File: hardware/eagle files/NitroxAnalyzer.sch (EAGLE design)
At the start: 16 parts

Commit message: Updated a bit the buttons hardware board to better match the 3d box
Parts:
- removed JP1: (no value), pinhead:PINHD-1X4
- removed JP11: (no value), pinhead:PINHD-1X3
- removed JP3, JP4: (no value), pinhead:PINHD-1X15
- added BUTTON_CON@2: (no value), pinhead:PINHD-1X3
- added OLED_CON: (no value), pinhead:PINHD-1X4
- added U$4: DIL30, ic-package:DIL30
- renumbered JP2 to BAT_CON, JP5 to FLUX_SENSOR_CON, JP8 to O2_CELL_CON, JP9 to BUTTONS_CON@1
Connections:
- new net N$10: U$4.5
- new net N$11: U$4.6
- new net N$12: U$4.9
- new net N$13: U$4.10
- new net N$14: U$4.11
- new net N$15: U$4.12
- new net N$16: U$4.13
- new net N$17: U$4.14
- new net N$18: U$4.15
- new net N$19: U$4.16
- new net N$2: U$4.1
- new net N$20: U$4.17
- new net N$21: U$4.18
- new net N$22: U$4.22
- new net N$23: U$4.25
- new net N$24: U$4.26
- new net N$25: U$4.28
- new net N$7: U$4.2
- new net N$9: U$4.3
- net +9V: now also U$4.30; no longer JP4.15
- net BATTERY_ANALOG: now also U$4.20; no longer JP4.5
- net CALIBRATE: now also U$4.8; no longer JP3.8
- net FLUX_ANALOG: now also U$4.21; no longer JP4.6
- net GND: now also OLED_CON.2, U$4.29, U$4.4; no longer JP1.2, JP3.4, JP4.14
- net N$4: now also BUTTON_CON@2.3; no longer JP11.3
- net N$6: now also BUTTON_CON@2.1; no longer JP11.1
- net N$8: now also BUTTON_CON@2.2; no longer JP11.2
- net O2_CELL_ANALOG: now also U$4.19; no longer JP4.4
- net SCL: now also OLED_CON.3, U$4.24; no longer JP1.3, JP4.9
- net SDA: now also OLED_CON.4, U$4.23; no longer JP1.4, JP4.8
- net START: now also U$4.7; no longer JP3.7
- net VCC: now also OLED_CON.1, U$4.27; no longer JP1.1, JP4.12
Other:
- moved on the sheet: CALIBRATE, START

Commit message: Updated some 3d cad models and other stuff
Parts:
- removed BAT_CON: (no value), pinhead:PINHD-1X2
- removed BUTTONS_CON@1: (no value), pinhead:PINHD-1X3
- removed OLED_CON: (no value), pinhead:PINHD-1X4
- added JP1: OLED_CON, pinhead:PINHD-1X4
- added JP2: BAT_CON, pinhead:PINHD-1X2
- added JP3: BUTTONS_CON@1, pinhead:PINHD-1X3
- JP4: value (none) -> BUTTON_CON@2
- JP5: value (none) -> O2_CELL_CON
- JP6: value (none) -> FLUX_SENSOR_CON
- renumbered BUTTON_CON@2 to JP4, FLUX_SENSOR_CON to JP6, O2_CELL_CON to JP5
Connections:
- net +9V: now also JP2.1; no longer BAT_CON.1
- net CALIBRATE: now also JP3.3; no longer BUTTONS_CON@1.3
- net GND: now also JP1.2, JP2.2, JP3.2; no longer BAT_CON.2, BUTTONS_CON@1.2, OLED_CON.2
- net SCL: now also JP1.3; no longer OLED_CON.3
- net SDA: now also JP1.4; no longer OLED_CON.4
- net START: now also JP3.1; no longer BUTTONS_CON@1.1
- net VCC: now also JP1.1; no longer OLED_CON.1
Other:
- moved on the sheet: U$4

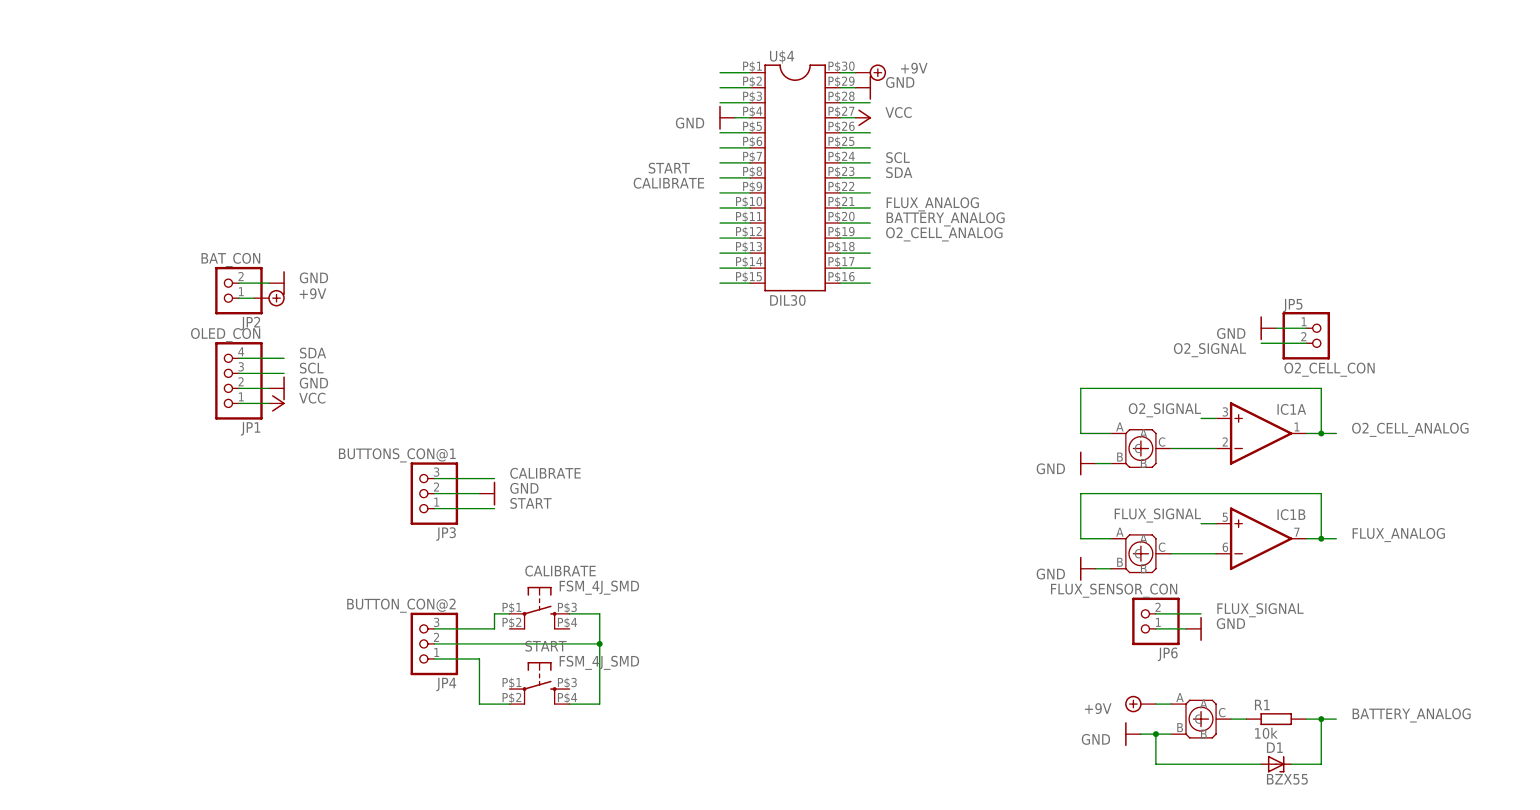
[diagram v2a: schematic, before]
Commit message: last commit on this solution.
I got some drawbacks that force to change the approach.

1- No more screen and buttons but an Android interface
2- Bluetooth Connection will be used
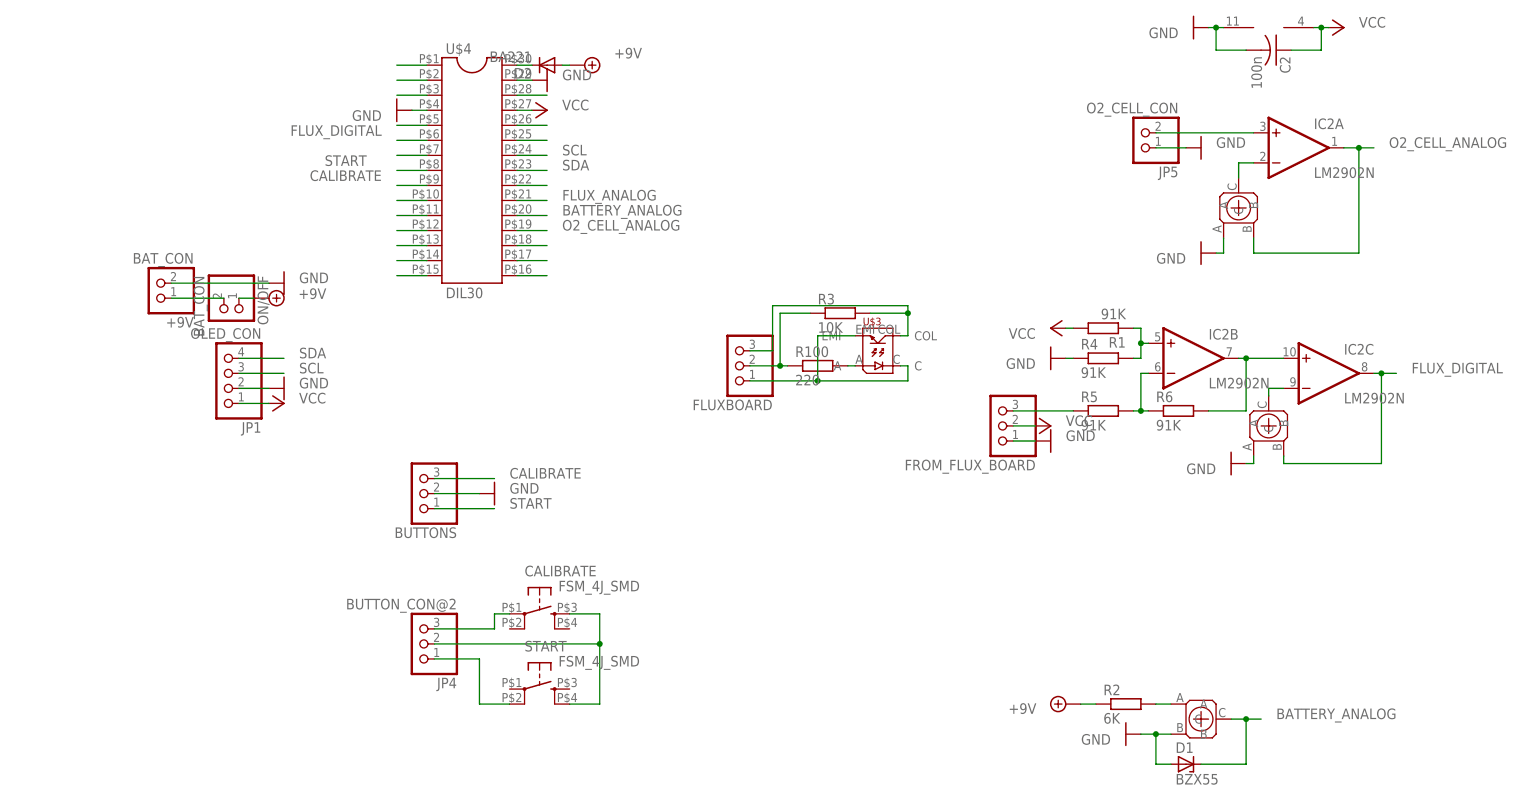
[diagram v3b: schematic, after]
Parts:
- removed IC1: (no value), linear:2AMP_P8+4N
- removed JP2: BAT_CON, pinhead:PINHD-1X2
- removed JP6: FLUX_SENSOR_CON, pinhead:PINHD-1X2
- added +9V, ON/OFF: BAT_CON, pinhead:PINHD-1X2
- added C2: 100n, rcl:C-USC1206
- added D2: BA221, diode:BA221
- added FLUXBOARD, FROM_FLUX_BOARD: (no value), pinhead:PINHD-1X3
- added IC2: LM2902N, linear:LM2902N
- added R100: 220, rcl:R-EU_R1206
- added R2: 6K, rcl:R-EU_R1206
- added R3: 10K, rcl:R-EU_R1206
- added R4, R5, R6: 91K, rcl:R-EU_R0805
- added U$5: 100K, piher:PT6KV
- BUTTONS: value BUTTONS_CON@1 -> (none)
- R1: value 10k -> 91K; device rcl:R-EU_R1206 -> rcl:R-EU_R0805
- U$1: value PT6KV-10k -> 10K
- U$2: value PT6KV-10k -> 100K
- U$3: value PT6KV-10k -> (none); device piher:PT6KV -> ITR8307:ITR8307
- renumbered JP3 to BUTTONS
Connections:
- removed net FLUX_SIGNAL: IC1B.+IN, JP6.2
- removed net O2_SIGNAL: IC1A.+IN, JP5.2
- new net FLUX_DIGITAL: IC2C.OUT, U$4.5, U$5.B
- new net GND_: FLUXBOARD.1, U$3.C, U$3.EMI
- new net N$26: R2.2, U$1.A
- new net N$28: IC2B.OUT, IC2C.+IN, R6.2
- new net N$29: IC2B.-IN, R5.2, R6.1
- new net N$30: FROM_FLUX_BOARD.3, R5.1
- new net N$31: IC2B.+IN, R1.1, R4.2
- new net N$32: IC2C.-IN, U$5.C
- new net N$33: IC2A.+IN, JP5.2
- new net SIG: FLUXBOARD.3, R3.2, U$3.COL
- new net VCC_: FLUXBOARD.2, R100.1, R3.1
- net +9V: now also D2.A, ON/OFF.1, R2.1; no longer JP2.1, U$1.A, U$4.30
- net BATTERY_ANALOG: now also U$1.C; no longer R1.2
- net FLUX_ANALOG: no longer IC1B.OUT, U$3.A
- net GND: now also +9V.2, C2.2, FROM_FLUX_BOARD.1, IC2P.V-, R4.1, U$2.A, U$5.A; no longer JP2.2, JP6.1, U$2.B, U$3.B
- net N$1: now also R100.2, U$3.A; no longer R1.1, U$1.C
- net N$10: now also D2.C, U$4.30; no longer U$4.5
- net N$3: now also IC2A.-IN; no longer IC1A.-IN
- net N$5: now also +9V.1, ON/OFF.2; no longer IC1B.-IN, U$3.C
- net O2_CELL_ANALOG: now also IC2A.OUT, U$2.B; no longer IC1A.OUT, U$2.A
- net VCC: now also C2.1, FROM_FLUX_BOARD.2, IC2P.V+, R1.2
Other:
- moved on the sheet: D1, JP5, R1, U$4
